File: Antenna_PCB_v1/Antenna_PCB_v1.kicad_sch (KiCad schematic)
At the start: 6 parts, among them J1 Conn_Coaxial_Power, J2 Conn_Coaxial_Power

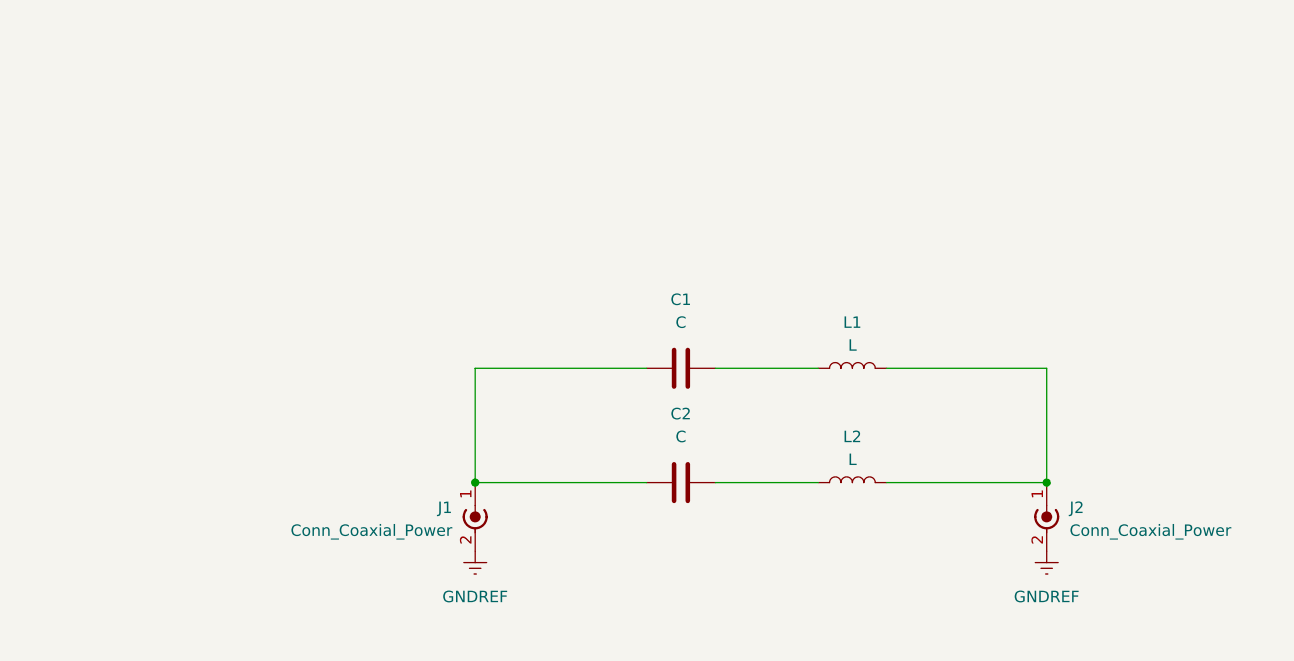
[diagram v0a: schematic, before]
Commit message: Add holes to PCB
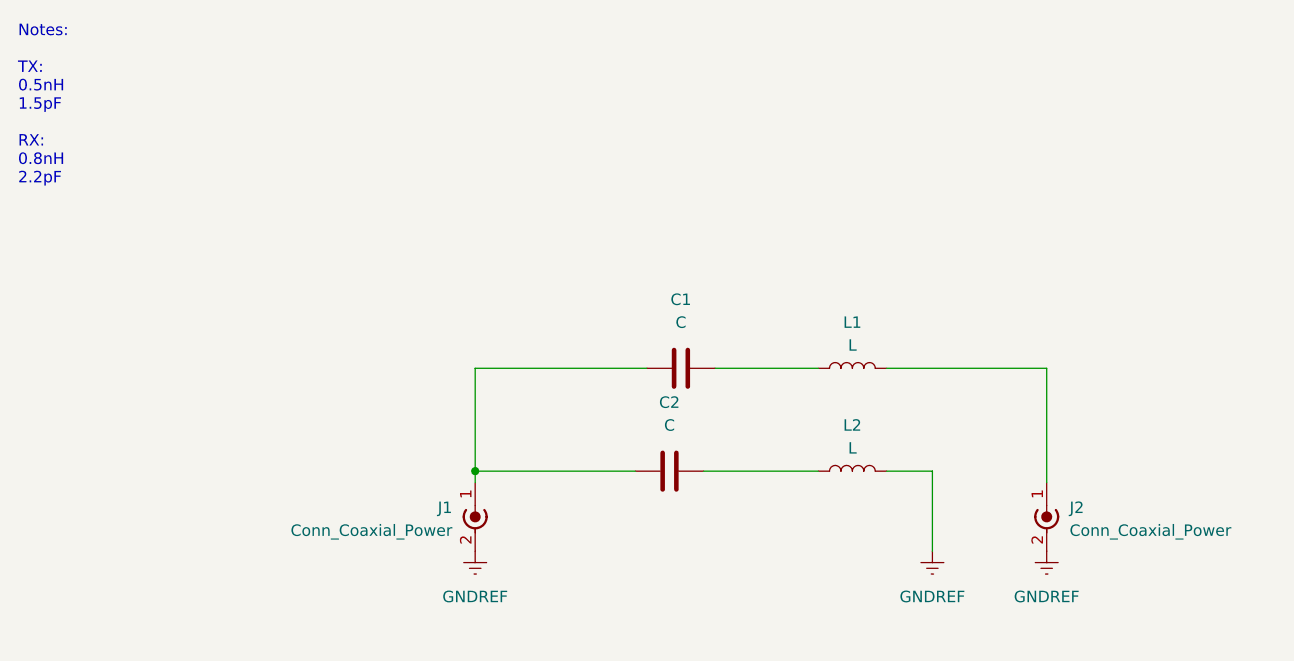
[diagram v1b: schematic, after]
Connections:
- net GNDREF: now also L2.2
- net at J2.1 (In), L1.2: no longer L2.2
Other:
- note added: "Notes: TX: 0.5nH 1.5pF RX: 0.8nH 2.2pF"
- title: (none) -> UA AIAA Payload 2026 Antenna PCB
- moved on the sheet: C2, L2
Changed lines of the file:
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@@
 	(generator_version "9.0")
 	(paper "A4")
+	(title_block
+		(title "UA AIAA Payload 2026 Antenna PCB")
+	)
+	(text "Notes:\n\nTX:\n0.5nH\n1.5pF\n\nRX:\n0.8nH\n2.2pF"
+		(exclude_from_sim no)
+		(at 12.7 12.7 0)
+		(effects
+			(font
+				(size 1.27 1.27)
+			)
+			(justify left top)
+		)
+	)
 	(junction
-		(at 63.5 63.5)
+		(at 63.5 62.23)
 		(diameter 0)
 		(color 0 0 0 0)
 	)
-	(junction
-		(at 127 63.5)
-		(diameter 0)
-		(color 0 0 0 0)
+	(wire
+		(pts
+			(xy 114.3 71.12) (xy 114.3 62.23)
+		)
+		(stroke
+			(width 0)
+			(type default)
+		)
 	)
 	(wire
@@
 	(wire
 		(pts
-			(xy 63.5 63.5) (xy 82.55 63.5)
-		)
-		(stroke
-			(width 0)
-			(type default)
-		)
-	)
-	(wire
-		(pts
-			(xy 101.6 63.5) (xy 90.17 63.5)
+			(xy 114.3 62.23) (xy 109.22 62.23)
+		)
+		(stroke
+			(width 0)
+			(type default)
+		)
+	)
+	(wire
+		(pts
+			(xy 81.28 62.23) (xy 63.5 62.23)
 		)
 		(stroke
@@
 	(wire
 		(pts
-			(xy 109.22 63.5) (xy 127 63.5)
-		)
-		(stroke
-			(width 0)
-			(type default)
-		)
-	)
-	(wire
-		(pts
 			(xy 127 50.8) (xy 127 63.5)
 		)
@@
 	(wire
 		(pts
-			(xy 63.5 50.8) (xy 63.5 63.5)
-		)
-		(stroke
-			(width 0)
-			(type default)
+			(xy 63.5 62.23) (xy 63.5 63.5)
+		)
+		(stroke
+			(width 0)
+			(type default)
+		)
+	)
+	(wire
+		(pts
+			(xy 63.5 50.8) (xy 63.5 62.23)
+		)
+		(stroke
+			(width 0)
+			(type default)
+		)
+	)
+	(wire
+		(pts
+			(xy 88.9 62.23) (xy 101.6 62.23)
+		)
+		(stroke
+			(width 0)
+			(type default)
+		)
+	)
+	(symbol
+		(lib_id "power:GNDREF")
+		(at 114.3 71.12 0)
+		(unit 1)
+		(exclude_from_sim no)
+		(in_bom yes)
+		(on_board yes)
+		(dnp no)
+		(fields_autoplaced yes)
+		(property "Reference" "#PWR03"
+			(at 114.3 77.47 0)
+			(effects
+				(font
+					(size 1.27 1.27)
+				)
+				(hide yes)
+			)
+		)
+		(property "Value" "GNDREF"
+			(at 114.3 76.2 0)
+			(effects
+				(font
+					(size 1.27 1.27)
+				)
+			)
+		)
+		(property "Footprint" ""
+			(at 114.3 71.12 0)
+			(effects
+				(font
+					(size 1.27 1.27)
+				)
+				(hide yes)
+			)
+		)
+		(property "Datasheet" ""
+			(at 114.3 71.12 0)
+			(effects
+				(font
+					(size 1.27 1.27)
+				)
+				(hide yes)
+			)
+		)
+		(property "Description" "Power symbol creates a global label with name \"GNDREF\" , reference supply ground"
+			(at 114.3 71.12 0)
+			(effects
+				(font
+					(size 1.27 1.27)
+				)
+				(hide yes)
+			)
+		)
+		(pin "1"
+		)
+		(instances
+			(project ""
+				(path "/5024d10e-9550-4469-87cc-7b555f45ca7d"
+					(reference "#PWR03")
+					(unit 1)
+				)
+			)
 		)
 	)
 	(symbol
 		(lib_id "Device:C")
-		(at 86.36 63.5 90)
+		(at 85.09 62.23 90)
 		(unit 1)
 		(exclude_from_sim no)
@@
 		(fields_autoplaced yes)
 		(property "Reference" "C2"
-			(at 86.36 55.88 90)
+			(at 85.09 54.61 90)
 			(effects
 				(font
@@
 		)
 		(property "Value" "C"
-			(at 86.36 58.42 90)
+			(at 85.09 57.15 90)
 			(effects
 				(font
@@
 		)
 		(property "Footprint" "Capacitor_SMD:C_0402_1005Metric"
-			(at 90.17 62.5348 0)
+			(at 88.9 61.2648 0)
 			(effects
 				(font
@@
 		)
 		(property "Datasheet" "~"
-			(at 86.36 63.5 0)
+			(at 85.09 62.23 0)
 			(effects
 				(font
@@
 		)
 		(property "Description" "Unpolarized capacitor"
-			(at 86.36 63.5 0)
+			(at 85.09 62.23 0)
 			(effects
 				(font
@@
 	(symbol
 		(lib_id "Device:L")
-		(at 105.41 63.5 90)
+		(at 105.41 62.23 90)
 		(unit 1)
 		(exclude_from_sim no)
@@
 		(fields_autoplaced yes)
 		(property "Reference" "L2"
-			(at 105.41 58.42 90)
+			(at 105.41 57.15 90)
 			(effects
 				(font
@@
 		)
 		(property "Value" "L"
-			(at 105.41 60.96 90)
+			(at 105.41 59.69 90)
 			(effects
 				(font
@@
 		)
 		(property "Footprint" "Inductor_SMD:L_0402_1005Metric"
-			(at 105.41 63.5 0)
+			(at 105.41 62.23 0)
 			(effects
 				(font
@@
 		)
 		(property "Datasheet" "~"
-			(at 105.41 63.5 0)
+			(at 105.41 62.23 0)
 			(effects
 				(font
@@
 		)
 		(property "Description" "Inductor"
-			(at 105.41 63.5 0)
-			(effects
-				(font
+			(at 105.41 62.23 0)
+			(effects
+				(font

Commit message: Fix antenna PCB circuit
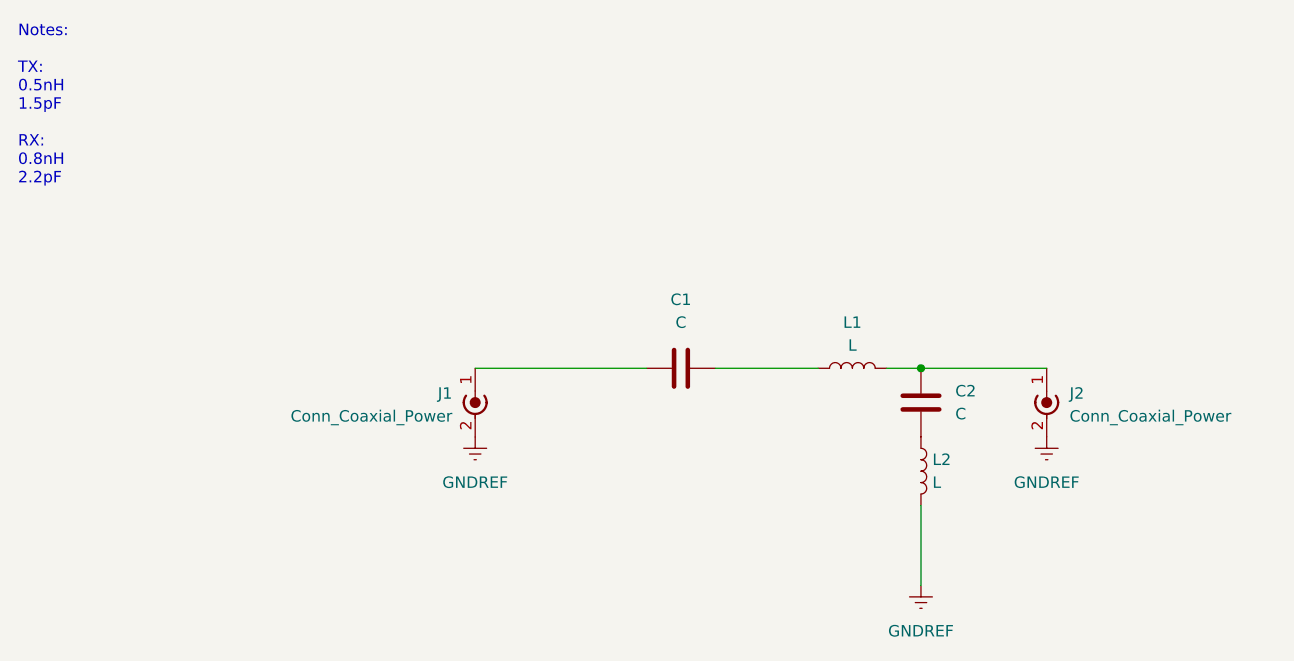
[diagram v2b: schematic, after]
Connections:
- net at C1.1, J1.1 (In): no longer C2.1
- net at J2.1 (In), L1.2: now also C2.1
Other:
- moved on the sheet: C2, J1, J2, L2
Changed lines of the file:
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@@
 	)
 	(junction
-		(at 63.5 62.23)
+		(at 113.03 50.8)
 		(diameter 0)
 		(color 0 0 0 0)
@@
 	(wire
 		(pts
-			(xy 114.3 71.12) (xy 114.3 62.23)
+			(xy 101.6 50.8) (xy 90.17 50.8)
 		)
 		(stroke
@@
 	(wire
 		(pts
-			(xy 101.6 50.8) (xy 90.17 50.8)
+			(xy 113.03 50.8) (xy 127 50.8)
 		)
 		(stroke
@@
 	(wire
 		(pts
-			(xy 114.3 62.23) (xy 109.22 62.23)
+			(xy 82.55 50.8) (xy 63.5 50.8)
 		)
 		(stroke
@@
 	(wire
 		(pts
-			(xy 81.28 62.23) (xy 63.5 62.23)
+			(xy 109.22 50.8) (xy 113.03 50.8)
 		)
 		(stroke
@@
 	(wire
 		(pts
-			(xy 82.55 50.8) (xy 63.5 50.8)
+			(xy 113.03 74.93) (xy 113.03 66.04)
 		)
 		(stroke
@@
 		)
 	)
-	(wire
-		(pts
-			(xy 127 50.8) (xy 127 63.5)
-		)
-		(stroke
-			(width 0)
-			(type default)
-		)
-	)
-	(wire
-		(pts
-			(xy 109.22 50.8) (xy 127 50.8)
-		)
-		(stroke
-			(width 0)
-			(type default)
-		)
-	)
-	(wire
-		(pts
-			(xy 63.5 62.23) (xy 63.5 63.5)
-		)
-		(stroke
-			(width 0)
-			(type default)
-		)
-	)
-	(wire
-		(pts
-			(xy 63.5 50.8) (xy 63.5 62.23)
-		)
-		(stroke
-			(width 0)
-			(type default)
-		)
-	)
-	(wire
-		(pts
-			(xy 88.9 62.23) (xy 101.6 62.23)
-		)
-		(stroke
-			(width 0)
-			(type default)
-		)
-	)
 	(symbol
 		(lib_id "power:GNDREF")
-		(at 114.3 71.12 0)
+		(at 113.03 74.93 0)
 		(unit 1)
 		(exclude_from_sim no)
@@
 		(fields_autoplaced yes)
 		(property "Reference" "#PWR03"
-			(at 114.3 77.47 0)
+			(at 113.03 81.28 0)
 			(effects
 				(font
@@
 		)
 		(property "Value" "GNDREF"
-			(at 114.3 76.2 0)
+			(at 113.03 80.01 0)
 			(effects
 				(font
@@
 		)
 		(property "Footprint" ""
-			(at 114.3 71.12 0)
+			(at 113.03 74.93 0)
 			(effects
 				(font
@@
 		)
 		(property "Datasheet" ""
-			(at 114.3 71.12 0)
+			(at 113.03 74.93 0)
 			(effects
 				(font
@@
 		)
 		(property "Description" "Power symbol creates a global label with name \"GNDREF\" , reference supply ground"
-			(at 114.3 71.12 0)
-			(effects
-				(font
-					(size 1.27 1.27)
-				)
-				(hide yes)
-			)
-		)
-		(pin "1"
-		)
-		(instances
-			(project ""
+			(at 113.03 74.93 0)
+			(effects
+				(font
+					(size 1.27 1.27)
+				)
+				(hide yes)
+			)
+		)
+		(pin "1"
+		)
+		(instances
+			(project "Antenna_PCB_v1"
 				(path "/5024d10e-9550-4469-87cc-7b555f45ca7d"
 					(reference "#PWR03")
@@
 	(symbol
 		(lib_id "Device:C")
-		(at 85.09 62.23 90)
+		(at 113.03 54.61 0)
 		(unit 1)
 		(exclude_from_sim no)
@@
 		(fields_autoplaced yes)
 		(property "Reference" "C2"
-			(at 85.09 54.61 90)
-			(effects
-				(font
-					(size 1.27 1.27)
-				)
+			(at 116.84 53.3399 0)
+			(effects
+				(font
+					(size 1.27 1.27)
+				)
+				(justify left)
 			)
 		)
 		(property "Value" "C"
-			(at 85.09 57.15 90)
-			(effects
-				(font
-					(size 1.27 1.27)
-				)
+			(at 116.84 55.8799 0)
+			(effects
+				(font
+					(size 1.27 1.27)
+				)
+				(justify left)
 			)
 		)
 		(property "Footprint" "Capacitor_SMD:C_0402_1005Metric"
-			(at 88.9 61.2648 0)
+			(at 113.9952 58.42 0)
 			(effects
 				(font
@@
 		)
 		(property "Datasheet" "~"
-			(at 85.09 62.23 0)
+			(at 113.03 54.61 0)
 			(effects
 				(font
@@
 		)
 		(property "Description" "Unpolarized capacitor"
-			(at 85.09 62.23 0)
+			(at 113.03 54.61 0)
 			(effects
 				(font
@@
 	(symbol
 		(lib_id "power:GNDREF")
-		(at 127 71.12 0)
+		(at 127 58.42 0)
 		(unit 1)
 		(exclude_from_sim no)
@@
 		(fields_autoplaced yes)
 		(property "Reference" "#PWR02"
-			(at 127 77.47 0)
+			(at 127 64.77 0)
 			(effects
 				(font
@@
 		)
 		(property "Value" "GNDREF"
-			(at 127 76.2 0)
+			(at 127 63.5 0)
 			(effects
 				(font
@@
 		)
 		(property "Footprint" ""
-			(at 127 71.12 0)
+			(at 127 58.42 0)
 			(effects
 				(font
@@
 		)
 		(property "Datasheet" ""
-			(at 127 71.12 0)
+			(at 127 58.42 0)
 			(effects
 				(font
@@
 		)
 		(property "Description" "Power symbol creates a global label with name \"GNDREF\" , reference supply ground"
-			(at 127 71.12 0)
+			(at 127 58.42 0)
 			(effects
 				(font
@@
 	(symbol
 		(lib_id "power:GNDREF")
-		(at 63.5 71.12 0)
+		(at 63.5 58.42 0)
 		(unit 1)
 		(exclude_from_sim no)
@@
 		(fields_autoplaced yes)
 		(property "Reference" "#PWR01"
-			(at 63.5 77.47 0)
+			(at 63.5 64.77 0)
 			(effects
 				(font
@@
 		)
 		(property "Value" "GNDREF"
-			(at 63.5 76.2 0)
+			(at 63.5 63.5 0)
 			(effects
 				(font
@@
 		)
 		(property "Footprint" ""
-			(at 63.5 71.12 0)
+			(at 63.5 58.42 0)
 			(effects
 				(font
@@
 		)
 		(property "Datasheet" ""
-			(at 63.5 71.12 0)
+			(at 63.5 58.42 0)
 			(effects
 				(font
@@
 		)
 		(property "Description" "Power symbol creates a global label with name \"GNDREF\" , reference supply ground"
-			(at 63.5 71.12 0)
+			(at 63.5 58.42 0)
 			(effects
 				(font
@@
 	(symbol
 		(lib_id "Connector:Conn_Coaxial_Power")
-		(at 63.5 66.04 0)
+		(at 63.5 53.34 0)
 		(mirror y)
 		(unit 1)
@@
 		(dnp no)
 		(property "Reference" "J1"
-			(at 60.96 66.2939 0)
+			(at 60.96 53.5939 0)
 			(effects
 				(font
@@
 		)
 		(property "Value" "Conn_Coaxial_Power"
-			(at 60.96 68.8339 0)
+			(at 60.96 56.1339 0)
 			(effects
 				(font
@@
 		)
 		(property "Footprint" "Connector_Coaxial:SMA_Molex_73251-1153_EdgeMount_Horizontal"
-			(at 63.5 67.31 0)
+			(at 63.5 54.61 0)
 			(effects
 				(font
@@
 		)
 		(property "Datasheet" "~"
-			(at 63.5 67.31 0)
+			(at 63.5 54.61 0)
 			(effects
 				(font
@@
 		)
 		(property "Description" "coaxial connector (BNC, SMA, SMB, SMC, Cinch/RCA, LEMO, ...)"
-			(at 63.5 66.04 0)
+			(at 63.5 53.34 0)
 			(effects
 				(font
@@
 	(symbol
 		(lib_id "Device:L")
-		(at 105.41 62.23 90)
+		(at 113.03 62.23 0)
 		(unit 1)
 		(exclude_from_sim no)
@@
 		(fields_autoplaced yes)
 		(property "Reference" "L2"
-			(at 105.41 57.15 90)
-			(effects
-				(font
-					(size 1.27 1.27)
-				)
+			(at 114.3 60.9599 0)
+			(effects
+				(font
+					(size 1.27 1.27)
+				)
+				(justify left)
 			)
 		)
 		(property "Value" "L"
-			(at 105.41 59.69 90)
-			(effects
-				(font
-					(size 1.27 1.27)
-				)
+			(at 114.3 63.4999 0)
+			(effects
+				(font
+					(size 1.27 1.27)
+				)
+				(justify left)
 			)
 		)
 		(property "Footprint" "Inductor_SMD:L_0402_1005Metric"
-			(at 105.41 62.23 0)
+			(at 113.03 62.23 0)
 			(effects
 				(font
@@
 		)
 		(property "Datasheet" "~"
-			(at 105.41 62.23 0)
+			(at 113.03 62.23 0)
 			(effects
 				(font
@@
 		)
 		(property "Description" "Inductor"
-			(at 105.41 62.23 0)
+			(at 113.03 62.23 0)
 			(effects
 				(font
@@
 	(symbol
 		(lib_id "Connector:Conn_Coaxial_Power")
-		(at 127 66.04 0)
+		(at 127 53.34 0)
 		(unit 1)
 		(exclude_from_sim no)
@@
 		(dnp no)
 		(property "Reference" "J2"
-			(at 129.54 66.2939 0)
+			(at 129.54 53.5939 0)
 			(effects
 				(font
@@
 		)
 		(property "Value" "Conn_Coaxial_Power"
-			(at 129.54 68.8339 0)
+			(at 129.54 56.1339 0)
 			(effects
 				(font
@@
 		)
 		(property "Footprint" "Connector_Coaxial:SMA_Molex_73251-1153_EdgeMount_Horizontal"
-			(at 127 67.31 0)
+			(at 127 54.61 0)
 			(effects
 				(font
@@
 		)
 		(property "Datasheet" "~"
-			(at 127 67.31 0)
+			(at 127 54.61 0)
 			(effects
 				(font
@@
 		)
 		(property "Description" "coaxial connector (BNC, SMA, SMB, SMC, Cinch/RCA, LEMO, ...)"
-			(at 127 66.04 0)
-			(effects
-				(font
+			(at 127 53.34 0)
+			(effects
+				(font

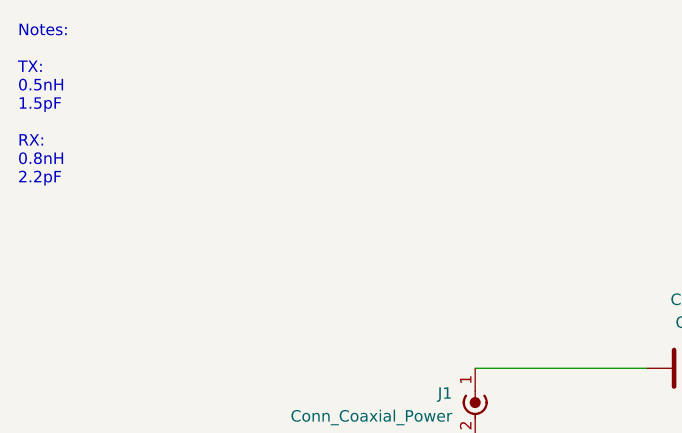
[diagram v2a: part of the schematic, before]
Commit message: Update antenna PCB 3D model
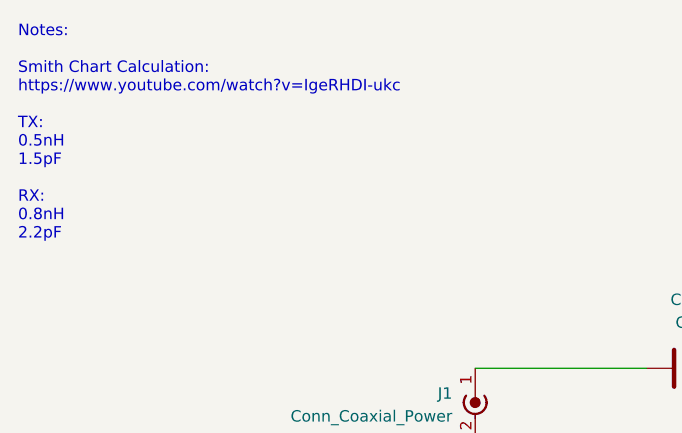
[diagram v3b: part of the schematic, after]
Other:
- note added: "Notes: Smith Chart Calculation: https://www.youtube.com/watch?v=IgeRHDI-ukc TX: 0.5nH 1.5pF RX: 0.8nH 2.2pF"
- note removed: "Notes: TX: 0.5nH 1.5pF RX: 0.8nH 2.2pF"
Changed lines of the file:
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@@
 		(title "UA AIAA Payload 2026 Antenna PCB")
 	)
-	(text "Notes:\n\nTX:\n0.5nH\n1.5pF\n\nRX:\n0.8nH\n2.2pF"
+	(text "Notes:\n\nSmith Chart Calculation:\nhttps://www.youtube.com/watch?v=IgeRHDI-ukc\n\nTX:\n0.5nH\n1.5pF\n\nRX:\n0.8nH\n2.2pF"
 		(exclude_from_sim no)
 		(at 12.7 12.7 0)
